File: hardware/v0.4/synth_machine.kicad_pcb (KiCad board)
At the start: 2 copper layers, 100 x 100 mm, 100 parts, among them J1 USB-C (MIDI + 5V power), J10 Pot VOL (10k lin, panel) JST-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, J11 Pot POT2 (10k lin, panel) JST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, J12 Pot POT3 (10k lin, panel) JST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, J13 Pot POT4 (10k lin, panel) JST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, J14 Pot POT5 (10k lin, panel) JST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, J15 STEMMA QT (I2C1), J5 Speaker L (JST-PH), J6 Speaker R (JST-PH), J7 Headphones 3.5mm (CUI SJ1-351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, J8 Expansion, J9 Display (SPI1), K1 KEY C4 (direct D10) JST-XH, K10 A4 [c2 r2] JST-XH, K11 A#4 [c1 r1] JST-XH, K12 B4 [c1 r2] JST-XH, K13 C5 [c0 r2] JST-XH, K14 BTN1 [c0 r0] JST-XH, K15 BTN2 [c0 r1] JST-XH, K16 BTN3 [c1 r0] JST-XH, K17 BTN4 [c2 r0] JST-XH, K18 BTN5 [c3 r0] JST-XH, K19 BTN6 [c4 r0] JST-XH, K2 C#4 [c5 r0] JST-XH, K3 D4 [c5 r1] JST-XH, K4 D#4 [c4 r1] JST-XH, K5 E4 [c5 r2] JST-XH, K6 F4 [c4 r2] JST-XH, K7 F#4 [c3 r1] JST-XH, K8 G4 [c3 r2] JST-XH, K9 G#4 [c2 r1] JST-XH, Q1 2N7002, Q2 2N7002, U1 Daisy Seed / Seed3, U2 TPA6138A2PWR, U3 MAX98306ETD+T, U4 USBLC6-2SC6

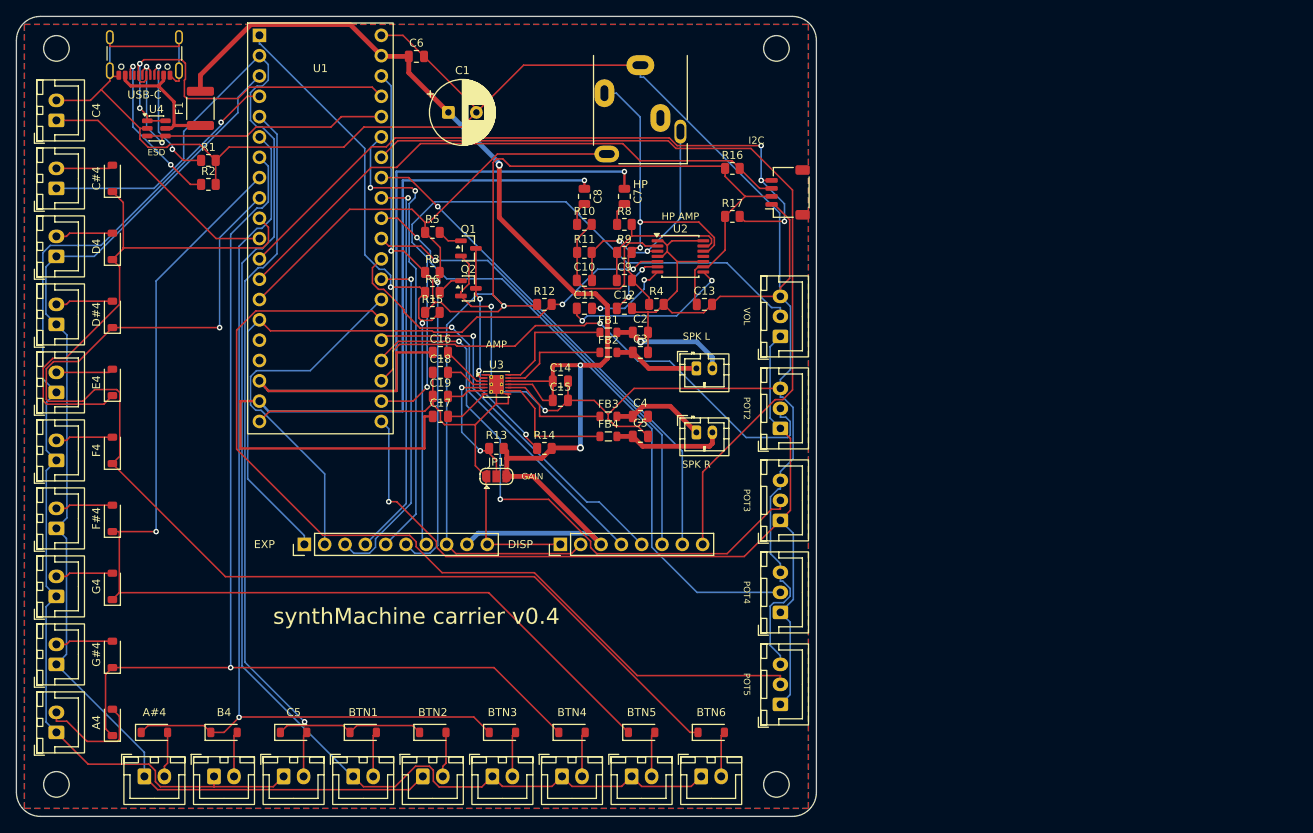
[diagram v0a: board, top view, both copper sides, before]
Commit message: Carrier v0.4: landscape board with one key row and onboard LiPo power
Rebuilt from the two remaining next-revision ideas (the RGB LED one is
dropped):

- 160 x 74 mm outline. All 19 key headers in one row along the bottom
  edge in panel order, rotated for a 7 mm pitch (132 mm wide), diode above
  each header and the key name below it. Pots stacked up the right edge,
  EXP and DISP headers along the top, mounting holes in the corners.
- Battery: BQ24074 charger with power path (1.5 A input limit via R19,
  0.5 A charge via R18, default timers, TS 10k), TPS61023 boost to 5.1 V
  (750k/100k, 1 uH XEL4030, 10 uF in, 2 x 22 uF out + C1), JST-PH cell on
  J17, panel power switch on J16 driving the boost's EN (JP2 bridges it),
  VBAT/2 to A10, ~CHG to A5, ~PGOOD to A11. Rails: VBUS -> F1 -> VUSB ->
  charger -> VSYS -> boost -> +5V.
- Generator: mpn/dnp per part kept; pre-routes added for the boost's
  SOT-563 pins, the output-cap link, the switch pull-up rail and nine GND
  stitching vias; battery rails in the 0.4 mm class, 0.15 mm clearance so
  0.5 mm pitch pads pass DRC.
- Routed (Freerouting 2.4.1): DRC 0 unconnected, ERC clean; fab.sh's
  PCBWay BOM now lists every fitted part.
- Docs: v0.4 README rewritten with the power section, pin map, headers and
  pre-order checks; NEXT_REVISION marks the key row and LiPo as done and
  drops the LED note; Digi-Key list adds the switch, battery and PH parts.

Co-Authored-By: Claude Fable 5.1 <noreply@anthropic.com>
Claude-Session: https://claude.ai/code/session_019ZDGV5fm4G7LwUwRWHEiwx
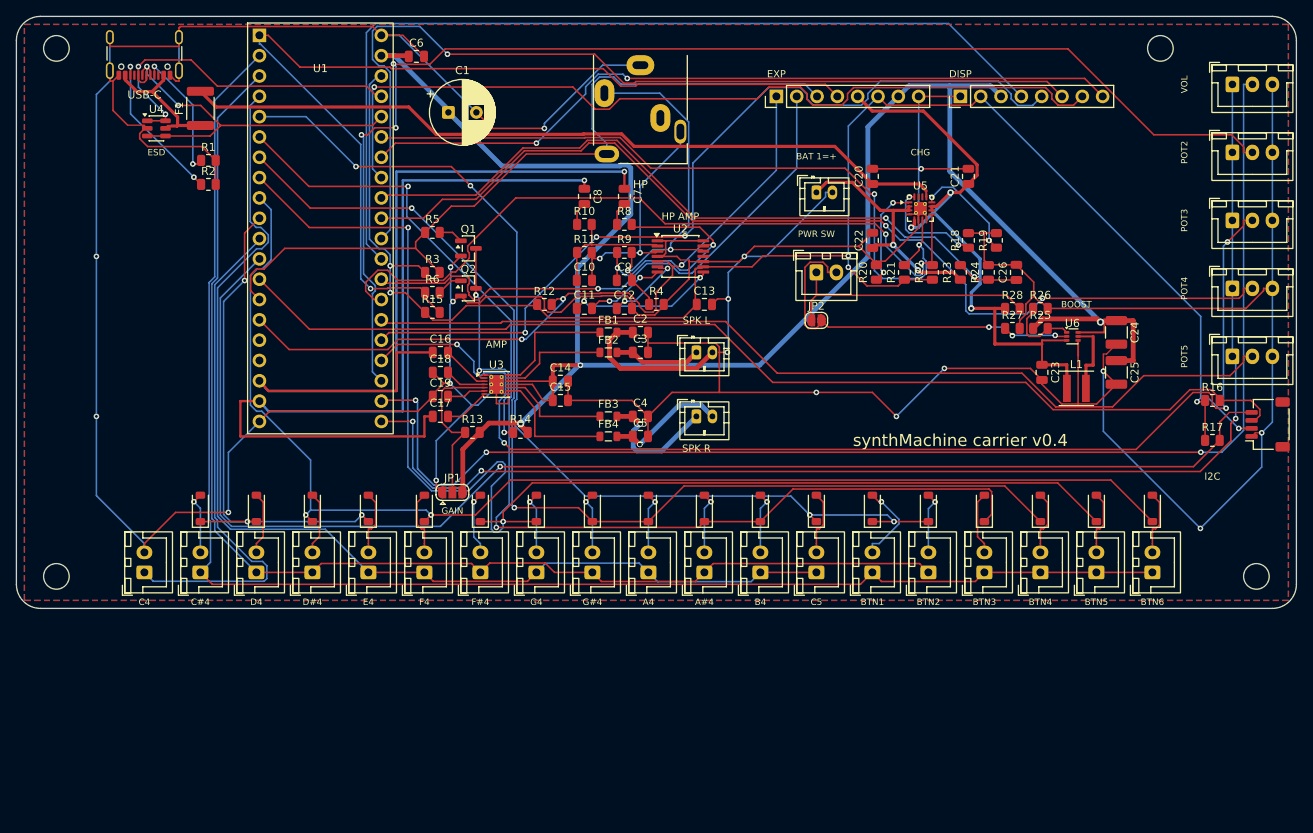
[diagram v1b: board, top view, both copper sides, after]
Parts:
- added C20: 1u, C_0805_2012Metric, F.Cu at (107.0, 20.0)
- added C21: 10u, C_0805_2012Metric, F.Cu at (119.0, 20.0)
- added C22: 10u, C_0805_2012Metric, F.Cu at (107.0, 28.0)
- added C23: 10u, C_0805_2012Metric, F.Cu at (128.2, 44.5)
- added C24: 22u 25V, C_1210_3225Metric, F.Cu at (137.5, 39.5)
- added C25: 22u 25V, C_1210_3225Metric, F.Cu at (137.5, 44.5)
- added C26: 100n, C_0805_2012Metric, F.Cu at (125.0, 32.0)
- added J16: Power switch (panel SPST) JST-XH, JST_XH_B2B-XH-A_1x02_P2.50mm_Vertical, F.Cu at (100.0, 32.0)
- added J17: Battery 1S LiPo (JST-PH, 1 = +), JST_PH_B2B-PH-K_1x02_P2.00mm_Vertical, F.Cu at (100.0, 22.0)
- added JP2: always on (bridges the power switch), SolderJumper-2_P1.3mm_Open_RoundedPad1.0x1.5mm, F.Cu at (100.0, 38.0)
- added L1: 1u 4x4 (XEL4030-102ME), L_Coilcraft_XxL4030, F.Cu at (132.5, 46.5)
- added R18: 1k8 (ISET 0.5A), R_0805_2012Metric, F.Cu at (119.0, 28.0)
- added R19: 1k1 (ILIM 1.5A), R_0805_2012Metric, F.Cu at (122.5, 28.0)
- added R20: 10k, R_0805_2012Metric, F.Cu at (107.5, 32.0)
- added R21: 100k, R_0805_2012Metric, F.Cu at (111.0, 32.0)
- added R22: 100k, R_0805_2012Metric, F.Cu at (114.5, 32.0)
- added R23: 100k, R_0805_2012Metric, F.Cu at (118.0, 32.0)
- added R24: 100k, R_0805_2012Metric, F.Cu at (121.5, 32.0)
- added R25: 750k (FB, 5.1V), R_0805_2012Metric, F.Cu at (128.0, 39.0)
- added R26: 100k, R_0805_2012Metric, F.Cu at (128.0, 36.5)
- added R27: 100k, R_0805_2012Metric, F.Cu at (124.5, 39.0)
- added R28: 10k, R_0805_2012Metric, F.Cu at (124.5, 36.5)
- added U5: BQ24074RGTR, VQFN-16-1EP_3x3mm_P0.5mm_EP1.6x1.6mm_ThermalVias, F.Cu at (113.0, 24.0)
- added U6: TPS61023DRLR, SOT-563, F.Cu at (132.0, 40.0)
- J8: footprint PinHeader_1x10_P2.54mm_Vertical -> PinHeader_1x08_P2.54mm_Vertical
- moved J8 81.3 mm to (95.0, 10.0)
- moved K10 76.7 mm to (79.0, 69.5)
- moved J9 75.1 mm to (118.0, 10.0)
- moved K11 74.5 mm to (86.0, 69.5), turned to 90 degrees
- moved D10 74.2 mm to (86.0, 61.5), turned to 90 degrees
- moved K12 72.9 mm to (93.0, 69.5), turned to 90 degrees
- moved D11 72.7 mm to (93.0, 61.5), turned to 90 degrees
- moved D9 72.1 mm to (79.0, 61.5)
- moved K13 71.3 mm to (100.0, 69.5), turned to 90 degrees
- moved J14 71.3 mm to (152.0, 42.5), turned to 0 degrees
- moved D12 71.1 mm to (100.0, 61.5), turned to 90 degrees
- moved K14 69.7 mm to (107.0, 69.5), turned to 90 degrees
- moved D13 69.5 mm to (107.0, 61.5), turned to 90 degrees
- moved J13 69.5 mm to (152.0, 34.0), turned to 0 degrees
- moved K15 68.2 mm to (114.0, 69.5), turned to 90 degrees
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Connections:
- F1 pad 2: +5V -> VUSB
- J8 pad 2: EXP_A5 -> EXP_A6
- J8 pad 3: EXP_A6 -> HP_DET
- J8 pad 4: EXP_A10 -> MUTE
- J8 pad 5: EXP_A11 -> VSYS
- J8 pad 6: HP_DET -> +3V3
- J8 pad 7: MUTE -> +5V
- J8 pad 8: +3V3 -> GND
- U1 pad 27: EXP_A5 -> CHG_STAT
- U1 pad 32: EXP_A10 -> VBAT_SENSE
- U1 pad 35: EXP_A11 -> USB_PGOOD
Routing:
- net GND: track 418.2 -> 697.0 mm, vias 2 -> 18
- net VUSB: track 0.00 -> 96.7 mm
- net CHG_STAT: track 0.00 -> 93.7 mm, vias 0 -> 2
- net POT_2: track 65.9 -> 158.8 mm, vias 1 -> 3
- net VBAT_SENSE: track 0.00 -> 91.9 mm, vias 0 -> 2
- net USB_PGOOD: track 0.00 -> 91.9 mm, vias 0 -> 2
- net +5V: track 162.6 -> 253.8 mm
- net I2C_SCL: track 87.2 -> 170.8 mm, vias 3 -> 1
- net POT_VOL: track 81.4 -> 164.3 mm, vias 1 -> 3
- net VSYS: track 0.00 -> 77.2 mm, vias 0 -> 3
- net POT_3: track 74.4 -> 148.8 mm, vias 2 -> 4
- net SPI_SCK: track 51.9 -> 115.2 mm, vias 1 -> 0
- net I2C_SDA: track 73.4 -> 136.6 mm
- net SPI_MOSI: track 47.4 -> 107.2 mm, vias 1 -> 3
- net EXP_A11: track 59.1 -> 0.00 mm, vias 2 -> 0
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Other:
- board size 100 x 100 mm -> 160 x 74 mm
- board text added: "BAT 1=+"
- board text added: "BOOST"
- board text added: "CHG"
- board text added: "PWR SW"

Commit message: Carrier v0.4: bank pots replaced by I2C encoders; volume pot only
J11..J14 are gone. J10 (volume, A0) stays on the right edge; the four bank
controls are seesaw rotary encoders on J15 (STEMMA QT, I2C1), now placed
mid-height on the right edge. A1/A2/A4/A9 go to the expansion header,
which grows to 1x12; DISP moves right to make room.

Pre-routes added for the charger's OUT and EN2 pins (0.5 mm pitch QFN) so
the VSYS rail always completes. Routed: DRC 0 unconnected, ERC clean.

Firmware HW=carrier4: reads A0 only and leaves the bank inputs alone (they
float without pots); encoder support is still to come. Docs, Digi-Key list
and NEXT_REVISION updated; the encoder item is marked done in hardware.

Co-Authored-By: Claude Fable 5.1 <noreply@anthropic.com>
Claude-Session: https://claude.ai/code/session_019ZDGV5fm4G7LwUwRWHEiwx
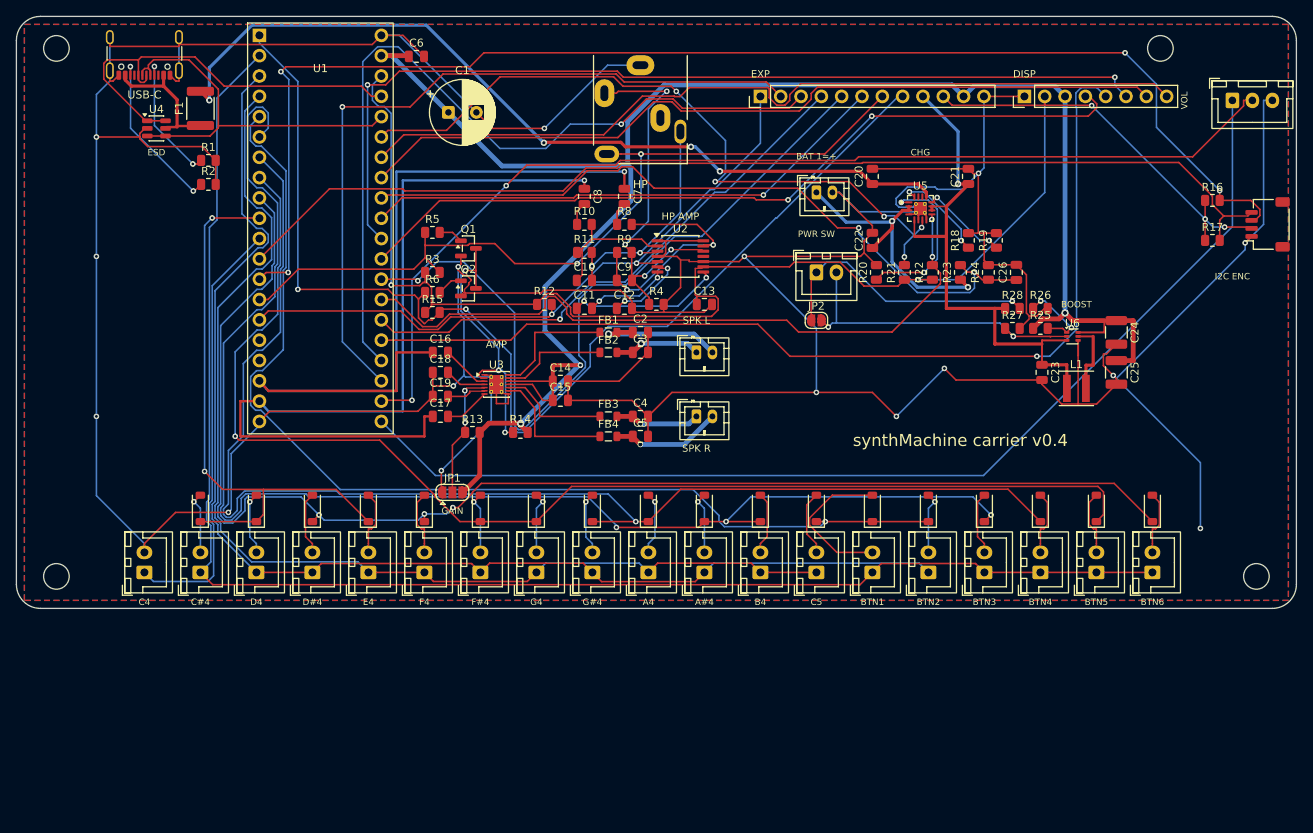
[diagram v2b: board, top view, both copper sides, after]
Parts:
- removed J11: Pot POT2 (10k lin, panel) JST-XH, JST_XH_B3B-XH-A_1x03_P2.50mm_Vertical
- removed J12: Pot POT3 (10k lin, panel) JST-XH, JST_XH_B3B-XH-A_1x03_P2.50mm_Vertical
- removed J13: Pot POT4 (10k lin, panel) JST-XH, JST_XH_B3B-XH-A_1x03_P2.50mm_Vertical
- removed J14: Pot POT5 (10k lin, panel) JST-XH, JST_XH_B3B-XH-A_1x03_P2.50mm_Vertical
- J8: footprint PinHeader_1x08_P2.54mm_Vertical -> PinHeader_1x12_P2.54mm_Vertical
- moved J15 25.0 mm to (156.4, 26.0)
- moved R16 25.0 mm to (149.5, 23.0)
- moved R17 25.0 mm to (149.5, 28.0)
- moved J9 8.00 mm to (126.0, 10.0)
- moved J10 2.00 mm to (152.0, 10.5)
- moved J8 2.00 mm to (93.0, 10.0)
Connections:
- J8 pad 2: EXP_A6 -> EXP_A1
- J8 pad 3: HP_DET -> EXP_A2
- J8 pad 4: MUTE -> EXP_A4
- J8 pad 5: VSYS -> EXP_A6
- J8 pad 6: +3V3 -> EXP_A9
- J8 pad 7: +5V -> HP_DET
- J8 pad 8: GND -> MUTE
- U1 pad 23: POT_2 -> EXP_A1
- U1 pad 24: POT_3 -> EXP_A2
- U1 pad 26: POT_5 -> EXP_A4
- U1 pad 31: POT_4 -> EXP_A9
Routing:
- net POT_2: track 158.8 -> 0.00 mm, vias 3 -> 0
- net POT_3: track 148.8 -> 0.00 mm, vias 4 -> 0
- net POT_4: track 125.2 -> 0.00 mm, vias 2 -> 0
- net POT_5: track 116.6 -> 0.00 mm
- net EXP_A2: track 0.00 -> 102.8 mm, vias 0 -> 1
- net EXP_A1: track 0.00 -> 93.9 mm, vias 0 -> 1
- net EXP_A4: track 0.00 -> 68.2 mm, vias 0 -> 1
- net EXP_A9: track 0.00 -> 66.4 mm, vias 0 -> 1
- net I2C_SCL: track 170.8 -> 136.1 mm, vias 1 -> 0
- net COL1: track 138.1 -> 170.7 mm, vias 2 -> 3
- net POT_VOL: track 164.3 -> 133.7 mm, vias 3 -> 2
- net I2C_SDA: track 136.6 -> 166.9 mm, vias 0 -> 4
- net COL2: track 134.8 -> 164.3 mm, vias 2 -> 1
- net EXP_A6: track 72.0 -> 99.0 mm
- net GND: track 697.0 -> 670.1 mm, vias 18 -> 16
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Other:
- board text added: "I2C ENC"
- board text removed: "I2C"
- board text removed: "POT2"
- board text removed: "POT3"
- board text removed: "POT4"
- board text removed: "POT5"

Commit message: Carrier v0.4: top-entry STEMMA QT at the top right, volume header on the left edge, jack 1.5 mm proud
- J15 becomes the vertical JST SH (BM04B-SRSS-TB, LCSC C160390) at the top
  right so the encoder cable leaves upward toward the panel; the DNP
  pull-ups follow it. Top-right mounting hole back at (155, 4).
- J10 (volume pot) moves to the left edge under the USB-C, matching where
  the pot sits on the panel.
- J7 headphone jack moved 1.5 mm toward the top edge; its nose now stands
  proud of the board edge instead of flush.
- One more pre-route (FB divider to +5V) so the boost cluster routes every
  time. DRC 0 unconnected, ERC clean.
- README: connector table, J15 pin-1 check, note that F1 and L1 only look
  empty in the render because KiCad has no 3D models for those footprints.

Co-Authored-By: Claude Fable 5.1 <noreply@anthropic.com>
Claude-Session: https://claude.ai/code/session_019ZDGV5fm4G7LwUwRWHEiwx
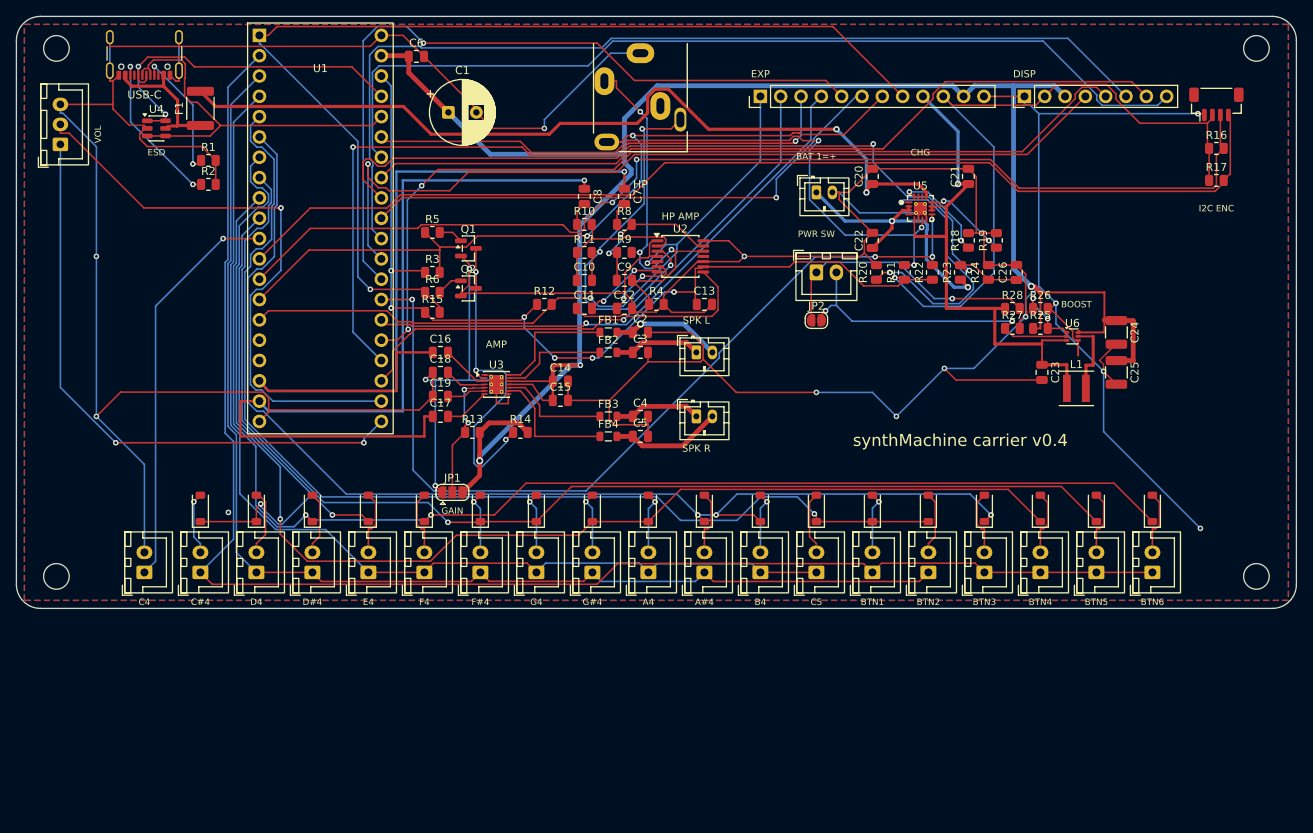
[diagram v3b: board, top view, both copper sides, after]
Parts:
- J15: footprint JST_SH_SM04B-SRSS-TB_1x04-1MP_P1.00mm_Horizontal -> JST_SH_BM04B-SRSS-TB_1x04-1MP_P1.00mm_Vertical
- moved J10 146.6 mm to (5.50, 16.0), turned to 90 degrees
- moved J15 16.3 mm to (150.0, 11.0), turned to 0 degrees
- moved H2 12.0 mm to (155.0, 4.00)
- moved R17 7.52 mm to (150.0, 20.5)
- moved R16 6.52 mm to (150.0, 16.5)
- moved J7 1.50 mm to (78.0, 4.60)
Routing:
- net +3.3VA: track 137.8 -> 74.7 mm, vias 0 -> 2
- net POT_VOL: track 133.7 -> 73.8 mm, vias 2 -> 1
- net I2C_SDA: track 166.9 -> 139.6 mm, vias 4 -> 2
- net COL1: track 170.7 -> 145.1 mm
- net EXP_A1: track 93.9 -> 70.8 mm
- net CHG_STAT: track 87.3 -> 110.1 mm, vias 2 -> 4
- net HP_R: track 29.7 -> 50.6 mm, vias 2 -> 3
- net MUTE: track 145.2 -> 132.3 mm, vias 2 -> 1
- net EXP_A2: track 102.8 -> 90.5 mm, vias 1 -> 2
- net TS: track 21.0 -> 32.8 mm
- net HP_INL: track 31.2 -> 19.6 mm
- net KBTN1_D: track 19.2 -> 7.83 mm, vias 0 -> 1
- net GND: track 670.1 -> 658.9 mm
- net SPI_MOSI: track 124.8 -> 114.1 mm, vias 1 -> 2
- net DISP_RST: track 105.6 -> 116.1 mm
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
